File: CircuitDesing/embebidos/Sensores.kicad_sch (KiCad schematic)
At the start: 6 parts

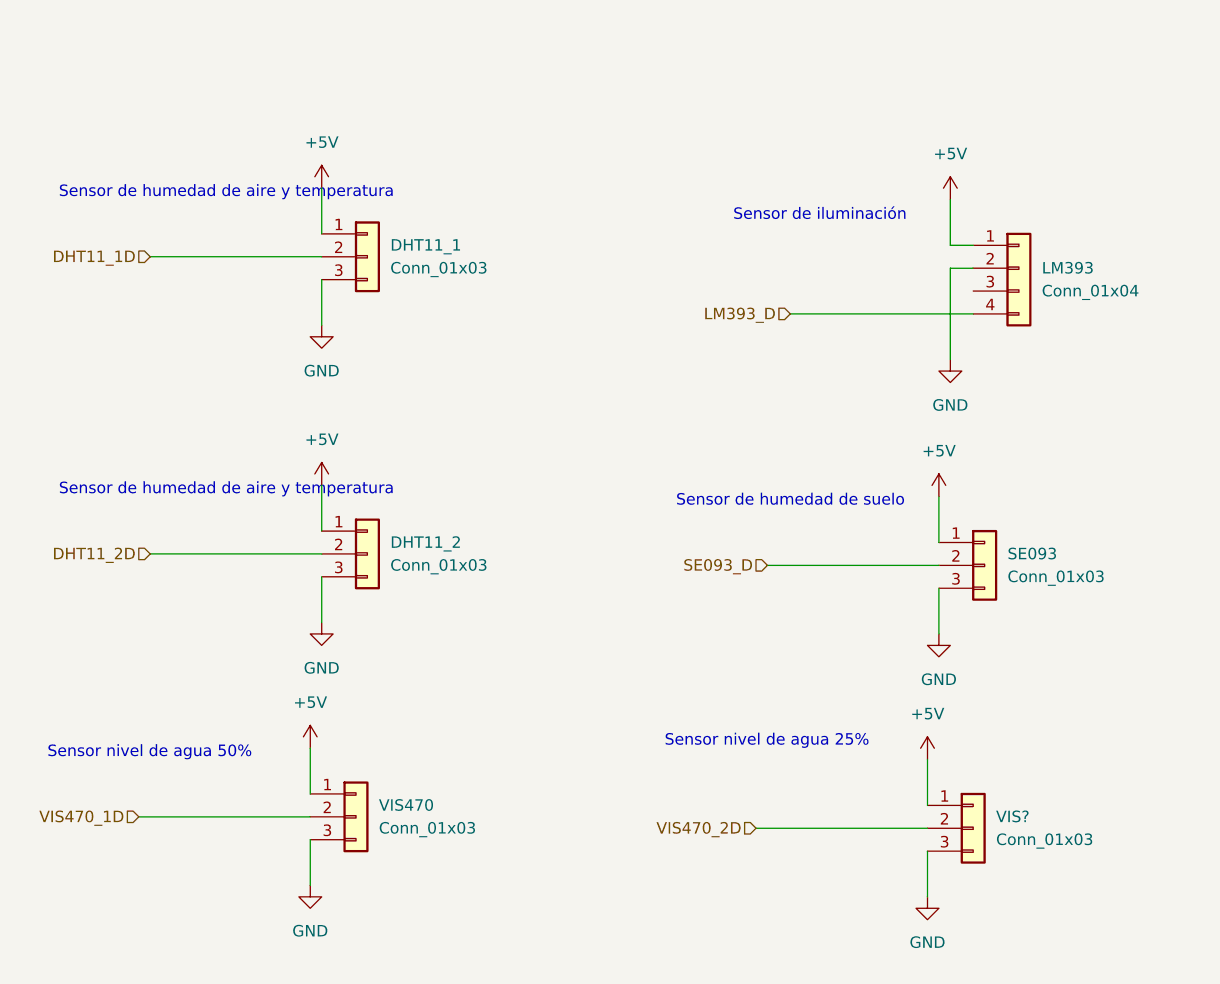
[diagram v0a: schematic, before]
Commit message: Potencia
Primera propuesta del esquema de potencia
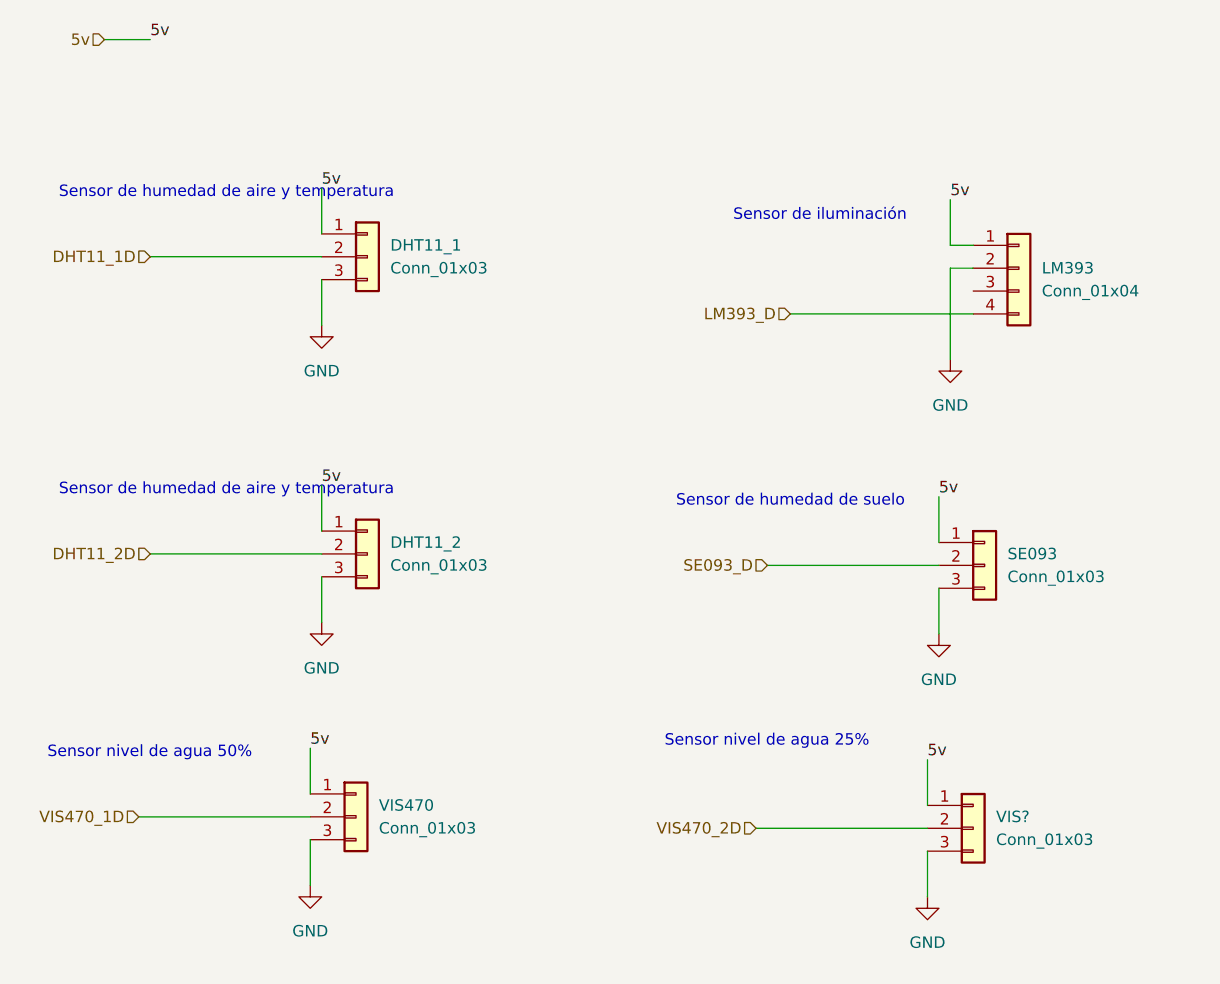
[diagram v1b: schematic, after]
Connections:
- net +5V renamed 5v
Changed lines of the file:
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@@
+    (stroke (width 0) (type default) (color 0 0 0 0))
+  )
+  (wire (pts (xy 45.72 40.64) (xy 50.8 40.64))
     (stroke (width 0) (type default) (color 0 0 0 0))
   )
@@
     (effects (font (size 1.27 1.27)) (justify left bottom))
   )
+  (label "5v" (at 68.58 119.38 0)
+    (effects (font (size 1.27 1.27)) (justify left bottom))
+  )
+  (label "5v" (at 139.7 58.42 0)
+    (effects (font (size 1.27 1.27)) (justify left bottom))
+  )
+  (label "5v" (at 50.8 40.64 0)
+    (effects (font (size 1.27 1.27)) (justify left bottom))
+  )
+  (label "5v" (at 69.85 57.15 0)
+    (effects (font (size 1.27 1.27)) (justify left bottom))
+  )
+  (label "5v" (at 69.85 90.17 0)
+    (effects (font (size 1.27 1.27)) (justify left bottom))
+  )
+  (label "5v" (at 137.16 120.65 0)
+    (effects (font (size 1.27 1.27)) (justify left bottom))
+  )
+  (label "5v" (at 138.43 91.44 0)
+    (effects (font (size 1.27 1.27)) (justify left bottom))
+  )
   (hierarchical_label "DHT11_1D" (shape input) (at 50.8 64.77 180)
     (effects (font (size 1.27 1.27)) (justify right))
@@
     (effects (font (size 1.27 1.27)) (justify right))
   )
+  (hierarchical_label "5v" (shape input) (at 45.72 40.64 180)
+    (effects (font (size 1.27 1.27)) (justify right))
+  )
   (hierarchical_label "VIS470_2D" (shape input) (at 118.11 128.27 180)
     (effects (font (size 1.27 1.27)) (justify right))
@@
     (pin "2")
     (pin "3")
-  )
-  (symbol (lib_id "power:+5V") (at 68.58 119.38 0) (unit 1)
-    (in_bom yes) (on_board yes) (fields_autoplaced)
-    (property "Reference" "#PWR?" (id 0) (at 68.58 123.19 0)
-      (effects (font (size 1.27 1.27)) hide)
-    )
-    (property "Value" "+5V" (id 1) (at 68.58 114.3 0))
-    (property "Footprint" "" (id 2) (at 68.58 119.38 0)
-      (effects (font (size 1.27 1.27)) hide)
-    )
-    (property "Datasheet" "" (id 3) (at 68.58 119.38 0)
-      (effects (font (size 1.27 1.27)) hide)
-    )
-    (pin "1")
   )
   (symbol (lib_id "power:GND") (at 137.16 135.89 0) (unit 1)
@@
     (pin "1")
   )
-  (symbol (lib_id "power:+5V") (at 138.43 91.44 0) (unit 1)
-    (in_bom yes) (on_board yes) (fields_autoplaced)
-    (property "Reference" "#PWR?" (id 0) (at 138.43 95.25 0)
-      (effects (font (size 1.27 1.27)) hide)
-    )
-    (property "Value" "+5V" (id 1) (at 138.43 86.36 0))
-    (property "Footprint" "" (id 2) (at 138.43 91.44 0)
-      (effects (font (size 1.27 1.27)) hide)
-    )
-    (property "Datasheet" "" (id 3) (at 138.43 91.44 0)
-      (effects (font (size 1.27 1.27)) hide)
-    )
-    (pin "1")
-  )
   (symbol (lib_id "Connector_Generic:Conn_01x03") (at 74.93 64.77 0) (unit 1)
     (in_bom yes) (on_board yes) (fields_autoplaced)
@@
     (pin "1")
   )
-  (symbol (lib_id "power:+5V") (at 69.85 57.15 0) (unit 1)
-    (in_bom yes) (on_board yes) (fields_autoplaced)
-    (property "Reference" "#PWR?" (id 0) (at 69.85 60.96 0)
-      (effects (font (size 1.27 1.27)) hide)
-    )
-    (property "Value" "+5V" (id 1) (at 69.85 52.07 0))
-    (property "Footprint" "" (id 2) (at 69.85 57.15 0)
-      (effects (font (size 1.27 1.27)) hide)
-    )
-    (property "Datasheet" "" (id 3) (at 69.85 57.15 0)
-      (effects (font (size 1.27 1.27)) hide)
-    )
-    (pin "1")
-  )
   (symbol (lib_id "Connector_Generic:Conn_01x04") (at 147.32 66.04 0) (unit 1)
     (in_bom yes) (on_board yes) (fields_autoplaced)
@@
     (pin "4")
   )
-  (symbol (lib_id "power:+5V") (at 137.16 120.65 0) (unit 1)
-    (in_bom yes) (on_board yes) (fields_autoplaced)
-    (property "Reference" "#PWR?" (id 0) (at 137.16 124.46 0)
-      (effects (font (size 1.27 1.27)) hide)
-    )
-    (property "Value" "+5V" (id 1) (at 137.16 115.57 0))
-    (property "Footprint" "" (id 2) (at 137.16 120.65 0)
-      (effects (font (size 1.27 1.27)) hide)
-    )
-    (property "Datasheet" "" (id 3) (at 137.16 120.65 0)
-      (effects (font (size 1.27 1.27)) hide)
-    )
-    (pin "1")
-  )
-  (symbol (lib_id "power:+5V") (at 139.7 58.42 0) (unit 1)
-    (in_bom yes) (on_board yes) (fields_autoplaced)
-    (property "Reference" "#PWR?" (id 0) (at 139.7 62.23 0)
-      (effects (font (size 1.27 1.27)) hide)
-    )
-    (property "Value" "+5V" (id 1) (at 139.7 53.34 0))
-    (property "Footprint" "" (id 2) (at 139.7 58.42 0)
-      (effects (font (size 1.27 1.27)) hide)
-    )
-    (property "Datasheet" "" (id 3) (at 139.7 58.42 0)
-      (effects (font (size 1.27 1.27)) hide)
-    )
-    (pin "1")
-  )
-  (symbol (lib_id "power:+5V") (at 69.85 90.17 0) (unit 1)
-    (in_bom yes) (on_board yes) (fields_autoplaced)
-    (property "Reference" "#PWR?" (id 0) (at 69.85 93.98 0)
-      (effects (font (size 1.27 1.27)) hide)
-    )
-    (property "Value" "+5V" (id 1) (at 69.85 85.09 0))
-    (property "Footprint" "" (id 2) (at 69.85 90.17 0)
-      (effects (font (size 1.27 1.27)) hide)
-    )
-    (property "Datasheet" "" (id 3) (at 69.85 90.17 0)
-      (effects (font (size 1.27 1.27)) hide)
-    )
-    (pin "1")
-  )
 )

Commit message: LDR
Comparacion LDR
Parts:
- removed LM393: Conn_01x04, symbol Connector_Generic:Conn_01x04
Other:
- added sheet Sensor de iluminacion (comparador_iluminacion.kicad_sch)
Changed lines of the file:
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@@
 (kicad_sch (version 20211123) (generator eeschema)
   (paper "A4")
-  (wire (pts (xy 139.7 66.04) (xy 139.7 76.2))
-    (stroke (width 0) (type default) (color 0 0 0 0))
-  )
   (wire (pts (xy 69.85 67.31) (xy 69.85 72.39))
     (stroke (width 0) (type default) (color 0 0 0 0))
   )
-  (wire (pts (xy 142.24 66.04) (xy 139.7 66.04))
-    (stroke (width 0) (type default) (color 0 0 0 0))
-  )
   (wire (pts (xy 69.85 57.15) (xy 69.85 62.23))
     (stroke (width 0) (type default) (color 0 0 0 0))
@@
     (stroke (width 0) (type default) (color 0 0 0 0))
   )
-  (wire (pts (xy 121.92 71.12) (xy 142.24 71.12))
-    (stroke (width 0) (type default) (color 0 0 0 0))
-  )
-  (wire (pts (xy 139.7 58.42) (xy 139.7 63.5))
+  (wire (pts (xy 111.76 59.69) (xy 111.76 64.77))
     (stroke (width 0) (type default) (color 0 0 0 0))
   )
@@
     (stroke (width 0) (type default) (color 0 0 0 0))
   )
+  (wire (pts (xy 120.65 68.58) (xy 113.03 68.58))
+    (stroke (width 0) (type default) (color 0 0 0 0))
+  )
   (wire (pts (xy 49.53 127) (xy 68.58 127))
     (stroke (width 0) (type default) (color 0 0 0 0))
@@
     (stroke (width 0) (type default) (color 0 0 0 0))
   )
-  (wire (pts (xy 139.7 63.5) (xy 142.24 63.5))
+  (wire (pts (xy 111.76 64.77) (xy 120.65 64.77))
     (stroke (width 0) (type default) (color 0 0 0 0))
   )
@@
     (effects (font (size 1.27 1.27)) (justify left bottom))
   )
-  (text "Sensor de iluminación" (at 115.57 60.96 0)
+  (text "Sensor de iluminación" (at 120.65 57.15 0)
     (effects (font (size 1.27 1.27)) (justify left bottom))
   )
@@
     (effects (font (size 1.27 1.27)) (justify left bottom))
   )
-  (label "5v" (at 139.7 58.42 0)
+  (label "5v" (at 111.76 59.69 0)
     (effects (font (size 1.27 1.27)) (justify left bottom))
   )
@@
     (effects (font (size 1.27 1.27)) (justify right))
   )
-  (hierarchical_label "LM393_D" (shape input) (at 121.92 71.12 180)
+  (hierarchical_label "LM393_D" (shape input) (at 113.03 68.58 180)
     (effects (font (size 1.27 1.27)) (justify right))
   )
@@
     (pin "1")
   )
-  (symbol (lib_id "power:GND") (at 139.7 76.2 0) (unit 1)
-    (in_bom yes) (on_board yes) (fields_autoplaced)
-    (property "Reference" "#PWR?" (id 0) (at 139.7 82.55 0)
-      (effects (font (size 1.27 1.27)) hide)
-    )
-    (property "Value" "GND" (id 1) (at 139.7 81.28 0))
-    (property "Footprint" "" (id 2) (at 139.7 76.2 0)
-      (effects (font (size 1.27 1.27)) hide)
-    )
-    (property "Datasheet" "" (id 3) (at 139.7 76.2 0)
-      (effects (font (size 1.27 1.27)) hide)
-    )
-    (pin "1")
-  )
   (symbol (lib_id "Connector_Generic:Conn_01x03") (at 74.93 97.79 0) (unit 1)
     (in_bom yes) (on_board yes) (fields_autoplaced)
@@
     (pin "1")
   )
-  (symbol (lib_id "Connector_Generic:Conn_01x04") (at 147.32 66.04 0) (unit 1)
-    (in_bom yes) (on_board yes) (fields_autoplaced)
-    (property "Reference" "LM393" (id 0) (at 149.86 66.0399 0)
-      (effects (font (size 1.27 1.27)) (justify left))
-    )
-    (property "Value" "Conn_01x04" (id 1) (at 149.86 68.5799 0)
-      (effects (font (size 1.27 1.27)) (justify left))
-    )
-    (property "Footprint" "" (id 2) (at 147.32 66.04 0)
-      (effects (font (size 1.27 1.27)) hide)
-    )
-    (property "Datasheet" "~" (id 3) (at 147.32 66.04 0)
-      (effects (font (size 1.27 1.27)) hide)
-    )
-    (pin "1")
-    (pin "2")
-    (pin "3")
-    (pin "4")
+  (sheet (at 120.65 60.96) (size 31.75 16.51) (fields_autoplaced)
+    (stroke (width 0.1524) (type solid) (color 0 0 0 0))
+    (fill (color 0 0 0 0.0000))
+    (property "Sheet name" "Sensor de iluminacion" (id 0) (at 120.65 60.2484 0)
+      (effects (font (size 1.27 1.27)) (justify left bottom))
+    )
+    (property "Sheet file" "comparador_iluminacion.kicad_sch" (id 1) (at 120.65 78.0546 0)
+      (effects (font (size 1.27 1.27)) (justify left top))
+    )
+    (pin "5v" input (at 120.65 64.77 180)
+      (effects (font (size 1.27 1.27)) (justify left))
+    )
+    (pin "Out" output (at 120.65 68.58 180)
+      (effects (font (size 1.27 1.27)) (justify left))
+    )
   )
 )
